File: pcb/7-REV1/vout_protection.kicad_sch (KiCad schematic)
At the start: 21 parts, among them Q3 PMXB56EN, Q4 PMXB56EN, Q6 2N7002T, U17 LM393BIDSGR

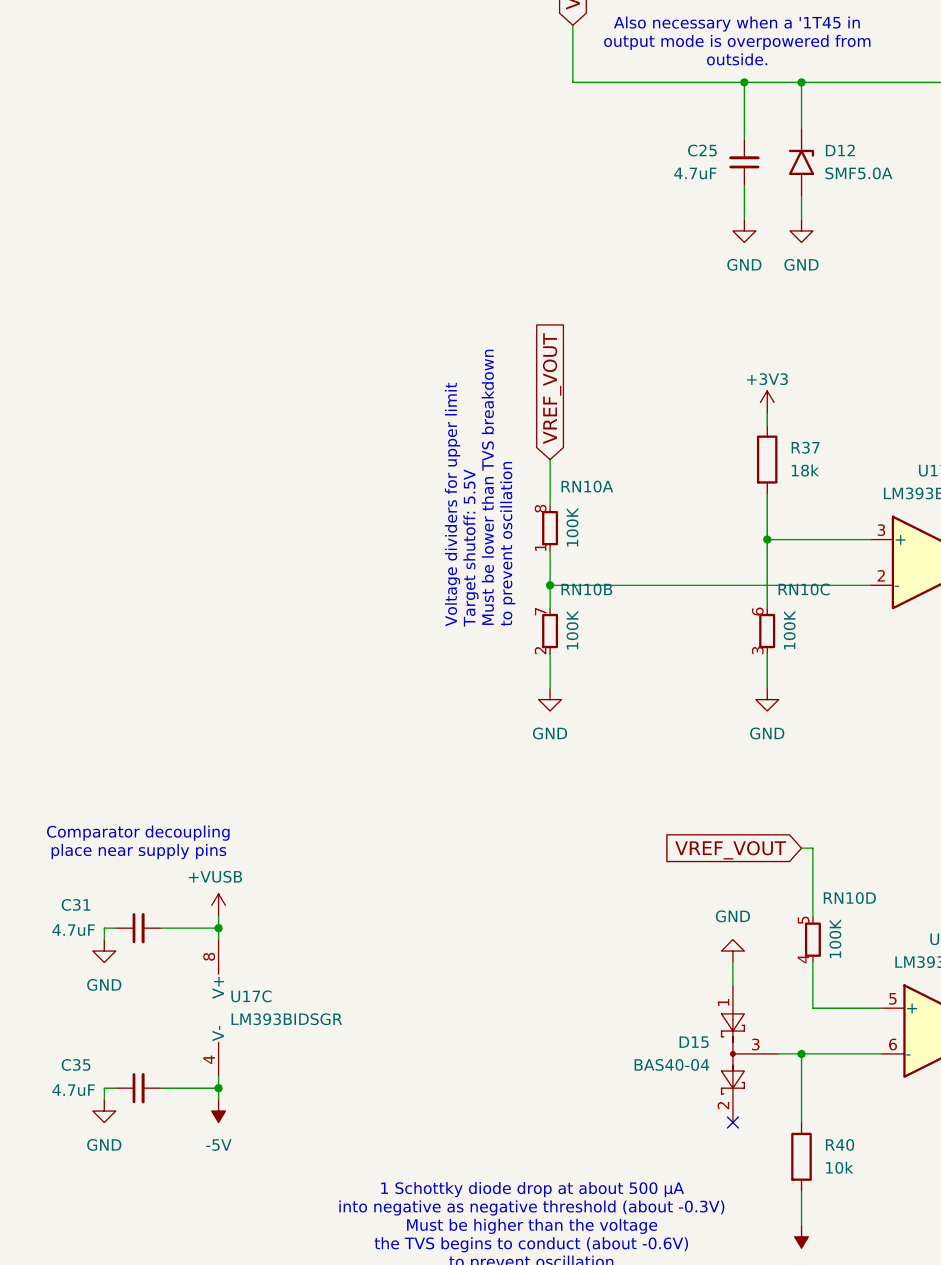
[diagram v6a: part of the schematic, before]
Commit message: BP7REV1 2.2uF, 4.7uF-> 10uF/6.3V CL05A106MQ5NUN. 520K->470K on reset/bootloader switch.
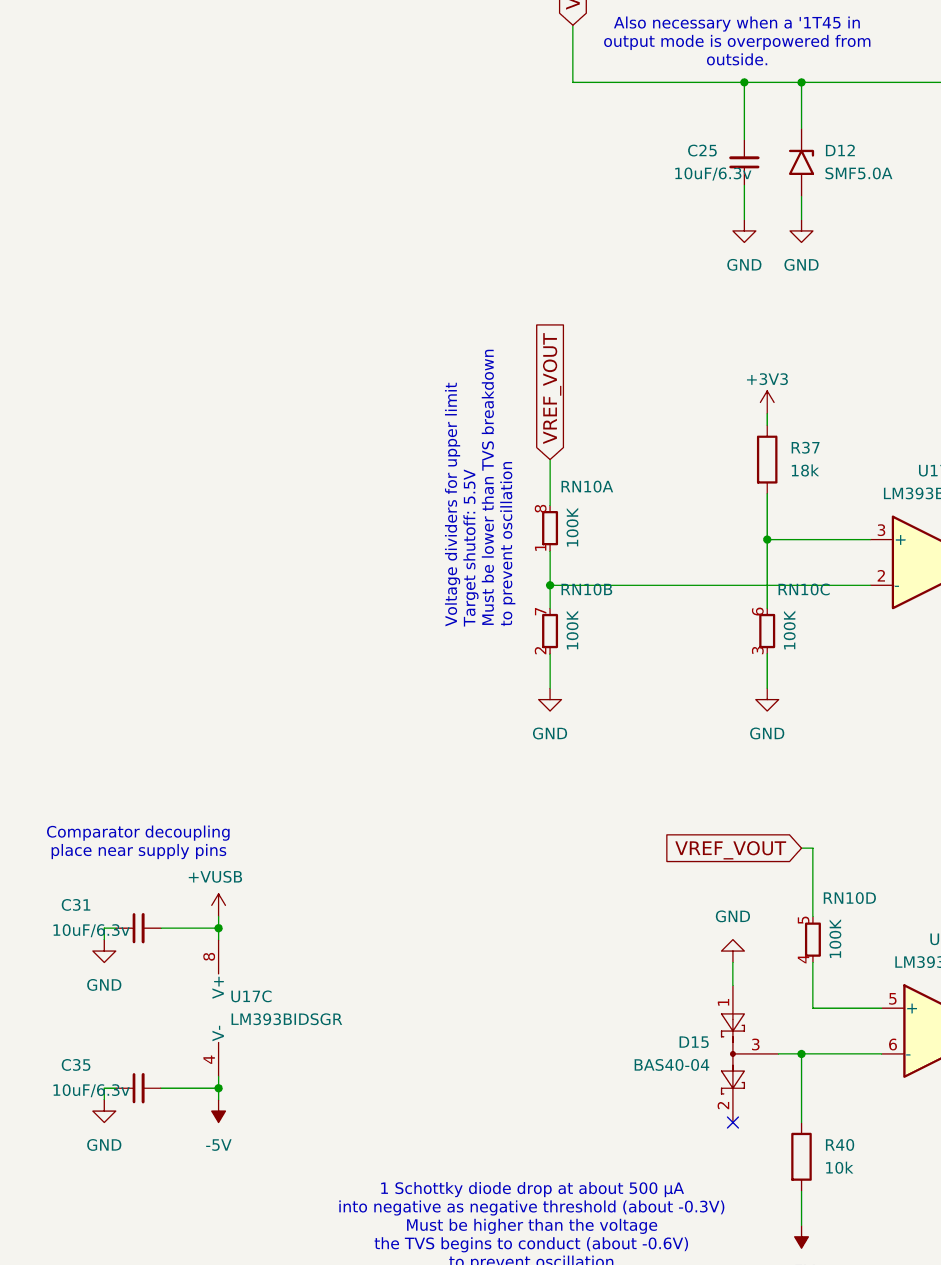
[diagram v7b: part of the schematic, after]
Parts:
- C25, C31, C35: value 4.7uF -> 10uF/6.3v
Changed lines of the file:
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@@
 			)
 		)
-		(property "Value" "4.7uF"
+		(property "Value" "10uF/6.3v"
 			(at 22.098 160.274 90)
 			(effects
@@
 			)
 		)
-		(property "Description" ""
+		(property "Description" "CL05A106MQ5NUN"
 			(at 31.75 160.02 0)
 			(effects
@@
 			)
 		)
-		(property "Value" "4.7uF"
+		(property "Value" "10uF/6.3v"
 			(at 22.098 142.494 90)
 			(effects
@@
 			)
 		)
-		(property "Description" ""
+		(property "Description" "CL05A106MQ5NUN"
 			(at 31.75 142.24 0)
 			(effects
@@
 			)
 		)
-		(property "Value" "4.7uF"
+		(property "Value" "10uF/6.3v"
 			(at 91.186 58.42 0)
 			(effects
@@
 			)
 		)
-		(property "Description" ""
+		(property "Description" "CL05A106MQ5NUN"
 			(at 99.06 57.15 0)
 			(effects

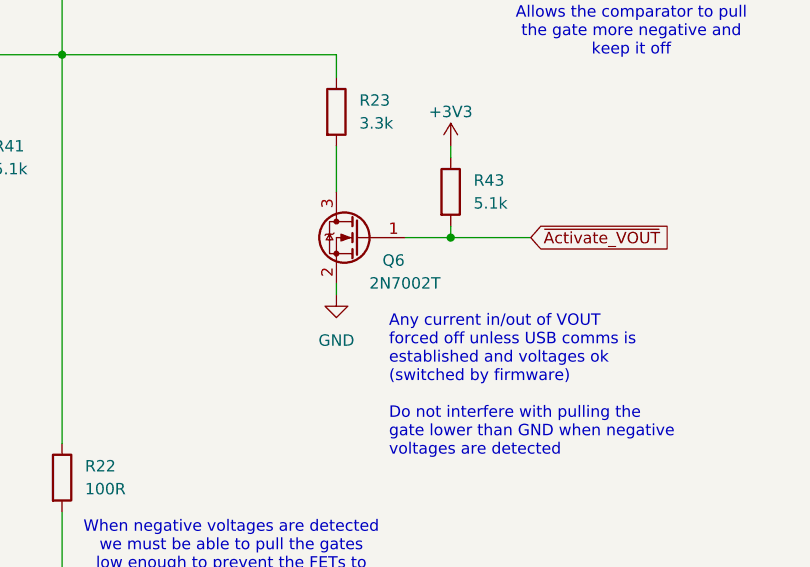
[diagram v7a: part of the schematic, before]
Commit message: specify part numbers and manufacturers in more detail - 10µF / 0805 caps - 2N7002KT fets
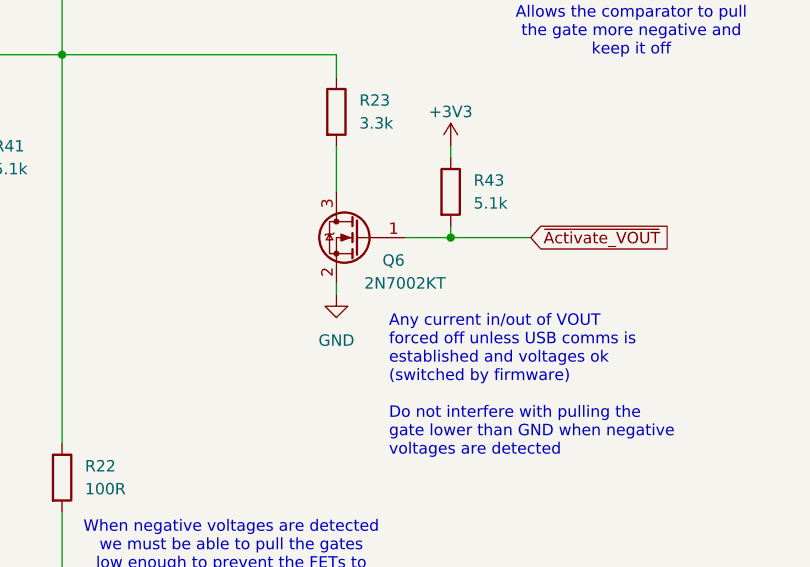
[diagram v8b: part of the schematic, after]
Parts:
- C25, C31, C35: MANUFACTURER (none) -> Samsung
- D13, Q3, Q4: MANUFACTURER (none) -> Nexperia
- Q6: value 2N7002T -> 2N7002KT; MANUFACTURER (none) -> CBI
